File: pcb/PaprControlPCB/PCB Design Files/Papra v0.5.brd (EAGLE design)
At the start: 36 x 45 mm, 40 parts, among them Q1 AO3400A (C20917), Q2 AO3400A (C20917), U1 LP2985-50DBVR (C74511), U2 ATTINYX04SOIC14

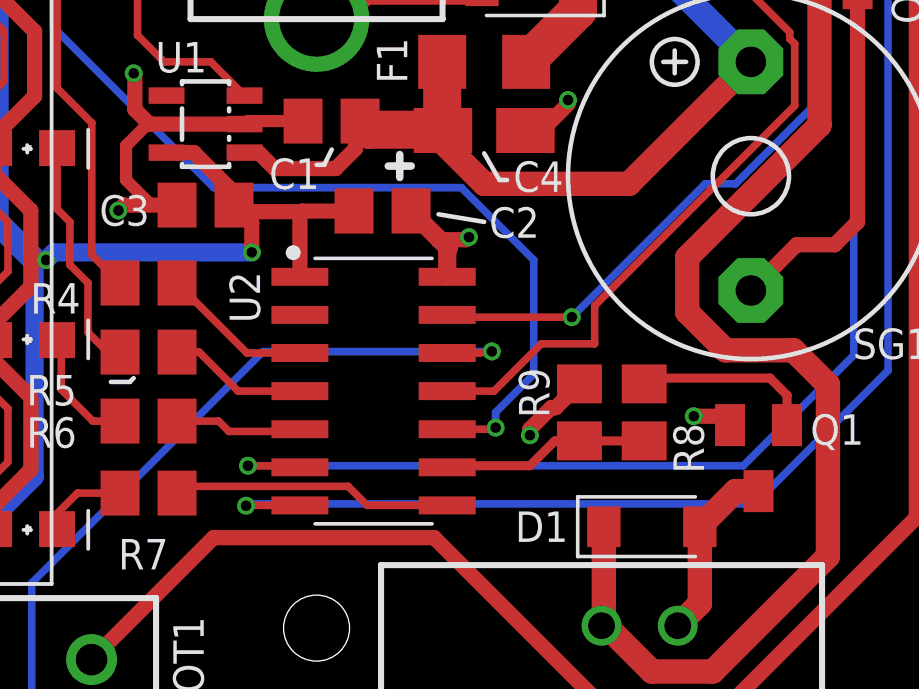
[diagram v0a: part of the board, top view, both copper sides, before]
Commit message: Moved Buzzer to W01 & LED4 to PA4
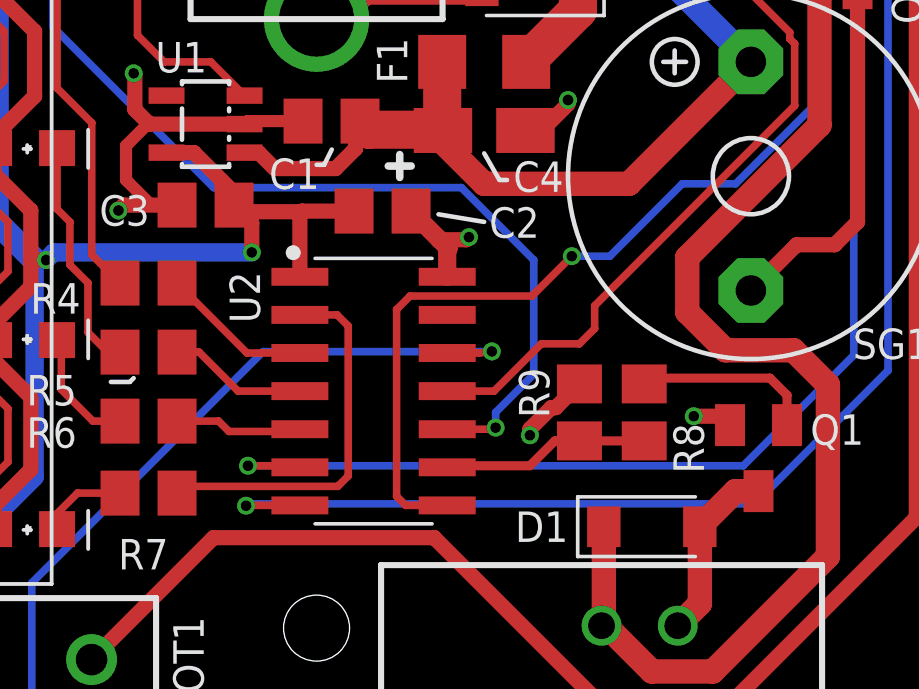
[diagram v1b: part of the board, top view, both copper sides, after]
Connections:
- net BUZZER: now also U2.8; no longer U2.13
- net LED4: now also U2.2; no longer U2.8
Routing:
- net BUZZER: track 28.7 -> 38.3 mm
- net LED4: track 9.36 -> 12.7 mm
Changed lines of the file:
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@@
 <layer number="14" name="Route14" color="22" fill="1" visible="no" active="no"/>
 <layer number="15" name="Route15" color="23" fill="1" visible="no" active="no"/>
-<layer number="16" name="Bottom" color="1" fill="1" visible="no" active="yes"/>
+<layer number="16" name="Bottom" color="1" fill="1" visible="yes" active="yes"/>
 <layer number="17" name="Pads" color="2" fill="1" visible="yes" active="yes"/>
 <layer number="18" name="Vias" color="2" fill="1" visible="yes" active="yes"/>
@@
 <layer number="43" name="vRestrict" color="2" fill="10" visible="no" active="yes"/>
 <layer number="44" name="Drills" color="7" fill="1" visible="no" active="yes"/>
-<layer number="45" name="Holes" color="7" fill="1" visible="no" active="yes"/>
+<layer number="45" name="Holes" color="7" fill="1" visible="yes" active="yes"/>
 <layer number="46" name="Milling" color="3" fill="1" visible="no" active="yes"/>
 <layer number="47" name="Measures" color="7" fill="1" visible="no" active="yes"/>
@@
 </layers>
 <board>
-<fusionsync huburn="a.YnVzaW5lc3M6Z21haWw5OTQ5MjA" projecturn="a.YnVzaW5lc3M6Z21haWw5OTQ5MjAjMjAyMDExMDYzNTA1MTIwMjY" f3durn="urn:adsk.wipprod:dm.lineage:bebFixbaRCeGagELh3PAVg" pcbguid="4d0b5712-029d-481f-ae2c-0115a28a8210" lastpulledtime="" lastsyncedchangeguid="" latestrevisionid="531739e1-a7f7-42f4-b71c-b58853c1dea1" lastsyncedrevisionid="531739e1-a7f7-42f4-b71c-b58853c1dea1" lastboardhashguid="b5928d42-975a-3bc9-637b-dc50c4e995b3" lastpushedtime="2021-04-26T01:24:42Z" linktopcb3d="true"/>
+<fusionsync huburn="a.YnVzaW5lc3M6Z21haWw5OTQ5MjA" projecturn="a.YnVzaW5lc3M6Z21haWw5OTQ5MjAjMjAyMDExMDYzNTA1MTIwMjY" f3durn="urn:adsk.wipprod:dm.lineage:bebFixbaRCeGagELh3PAVg" pcbguid="" lastpulledtime="" lastsyncedchangeguid="" latestrevisionid="531739e1-a7f7-42f4-b71c-b58853c1dea1" lastsyncedrevisionid="531739e1-a7f7-42f4-b71c-b58853c1dea1" lastboardhashguid="b5928d42-975a-3bc9-637b-dc50c4e995b3" lastpushedtime="2021-04-26T01:24:42Z" linktopcb3d="true"/>
 <plain>
 <wire x1="19.5" y1="22.5" x2="-13.5" y2="22.5" width="0.001" layer="20"/>
@@
 <wire x1="15.7734" y1="8.6440625" x2="15.9385" y2="8.4789625" width="0.254" layer="1"/>
 <wire x1="15.9385" y1="8.4789625" x2="15.9385" y2="6.4135" width="0.254" layer="1"/>
-<wire x1="9.271" y1="-0.254" x2="9.271" y2="-1.524" width="0.254" layer="1"/>
+<wire x1="9.271" y1="-0.254" x2="9.271" y2="-1.016" width="0.254" layer="1"/>
+<wire x1="9.271" y1="-1.016" x2="8.763" y2="-1.524" width="0.254" layer="1"/>
+<wire x1="8.763" y1="-1.524" x2="7.493" y2="-1.524" width="0.254" layer="1"/>
 <wire x1="5.917" y1="-3.1" x2="4.3554" y2="-3.1" width="0.254" layer="1"/>
 <wire x1="15.9385" y1="6.4135" x2="9.271" y2="-0.254" width="0.254" layer="1"/>
-<wire x1="9.271" y1="-1.524" x2="7.493" y2="-1.524" width="0.254" layer="1"/>
 <wire x1="7.493" y1="-1.524" x2="5.917" y2="-3.1" width="0.254" layer="1"/>
 </signal>
@@
 <signal name="LED4">
 <contactref element="R7" pad="2"/>
-<contactref element="U2" pad="8"/>
-<wire x1="1.6884" y1="-6.91" x2="4.3554" y2="-6.91" width="0.254" layer="1"/>
-<wire x1="1.6884" y1="-6.91" x2="1.0534" y2="-6.275" width="0.254" layer="1"/>
-<wire x1="1.0534" y1="-6.275" x2="-4.425" y2="-6.275" width="0.254" layer="1"/>
+<wire x1="1.0534" y1="-0.9264" x2="1.0534" y2="-5.9316" width="0.254" layer="1"/>
+<wire x1="1.0534" y1="-5.9316" x2="0.71" y2="-6.275" width="0.254" layer="1"/>
+<wire x1="0.71" y1="-6.275" x2="-4.425" y2="-6.275" width="0.254" layer="1"/>
 <wire x1="-4.65" y1="-6.5" x2="-4.425" y2="-6.275" width="0.254" layer="1"/>
+<contactref element="U2" pad="2"/>
+<wire x1="-0.5554" y1="-0.56" x2="0.687" y2="-0.56" width="0.254" layer="1"/>
+<wire x1="0.687" y1="-0.56" x2="1.0534" y2="-0.9264" width="0.254" layer="1"/>
 </signal>
 <signal name="LED1-R">
@@
 <contactref element="R12" pad="2"/>
 <contactref element="R13" pad="2"/>
-<contactref element="U2" pad="13"/>
 <via x="14.605" y="15.24" extent="1-16" drill="0.35"/>
 <wire x1="14.605" y1="15.24" x2="16.637" y2="13.208" width="0.254" layer="16"/>
-<wire x1="8.509" y1="-0.635" x2="12.954" y2="3.81" width="0.254" layer="16"/>
+<wire x1="12.192" y1="3.81" x2="9.779" y2="1.397" width="0.254" layer="16"/>
+<wire x1="8.509" y1="1.397" x2="9.779" y2="1.397" width="0.254" layer="16"/>
 <wire x1="16.637" y1="13.208" x2="16.637" y2="6.477" width="0.254" layer="16"/>
 <wire x1="16.637" y1="6.477" x2="13.97" y2="3.81" width="0.254" layer="16"/>
-<wire x1="13.97" y1="3.81" x2="12.954" y2="3.81" width="0.254" layer="16"/>
-<via x="8.509" y="-0.635" extent="1-16" drill="0.35"/>
-<wire x1="8.509" y1="-0.635" x2="4.4304" y2="-0.635" width="0.254" layer="1"/>
-<wire x1="4.4304" y1="-0.635" x2="4.3554" y2="-0.56" width="0.254" layer="1"/>
+<wire x1="13.97" y1="3.81" x2="12.192" y2="3.81" width="0.254" layer="16"/>
+<via x="8.509" y="1.397" extent="1-16" drill="0.35"/>
 <wire x1="16.068" y1="14.986" x2="15.814" y2="15.24" width="0.254" layer="1"/>
 <wire x1="15.814" y1="15.24" x2="14.605" y2="15.24" width="0.254" layer="1"/>
 <wire x1="16.068" y1="17.272" x2="16.068" y2="14.986" width="0.3048" layer="1"/>
+<contactref element="U2" pad="8"/>
+<wire x1="4.3554" y1="-6.91" x2="2.973" y2="-6.91" width="0.254" layer="1"/>
+<wire x1="2.973" y1="-6.91" x2="2.667" y2="-6.604" width="0.254" layer="1"/>
+<wire x1="2.667" y1="-6.604" x2="2.667" y2="-0.381" width="0.254" layer="1"/>
+<wire x1="3.11775" y1="0.06975" x2="7.18175" y2="0.06975" width="0.254" layer="1"/>
+<wire x1="7.18175" y1="0.06975" x2="8.509" y2="1.397" width="0.254" layer="1"/>
+<wire x1="2.667" y1="-0.381" x2="3.11775" y2="0.06975" width="0.254" layer="1"/>
 </signal>
 <signal name="BUZZER-GND" class="1">

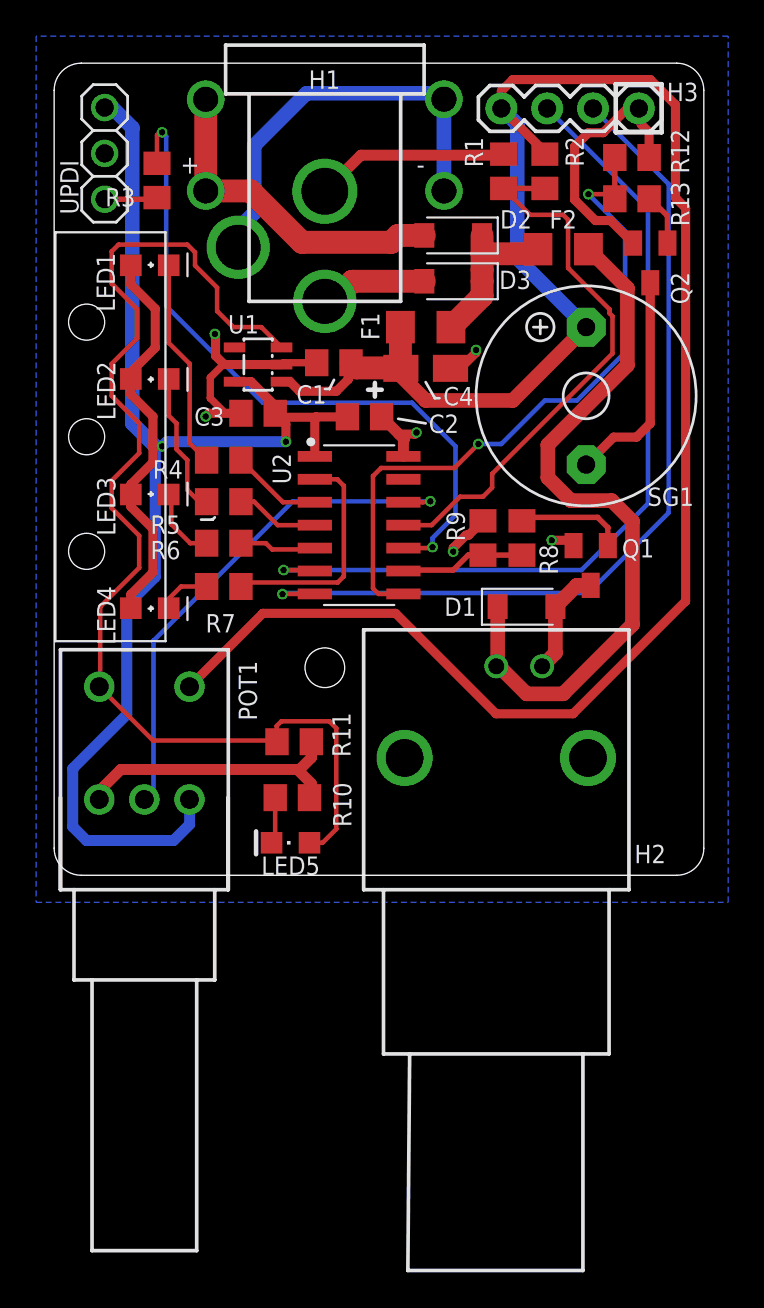
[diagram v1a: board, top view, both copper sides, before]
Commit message: Releasing to OSH
- Fixed for JLC DRU
- Unused pin tied to via & labeled PA3
- Adding 2 vias to allow shorting the UPDI resistor for use with programmers that have the UPDI in-circuit
- Tied the posts on the BNC together (can't tie to ground as we are switching ground)
- Silkscreen touchups
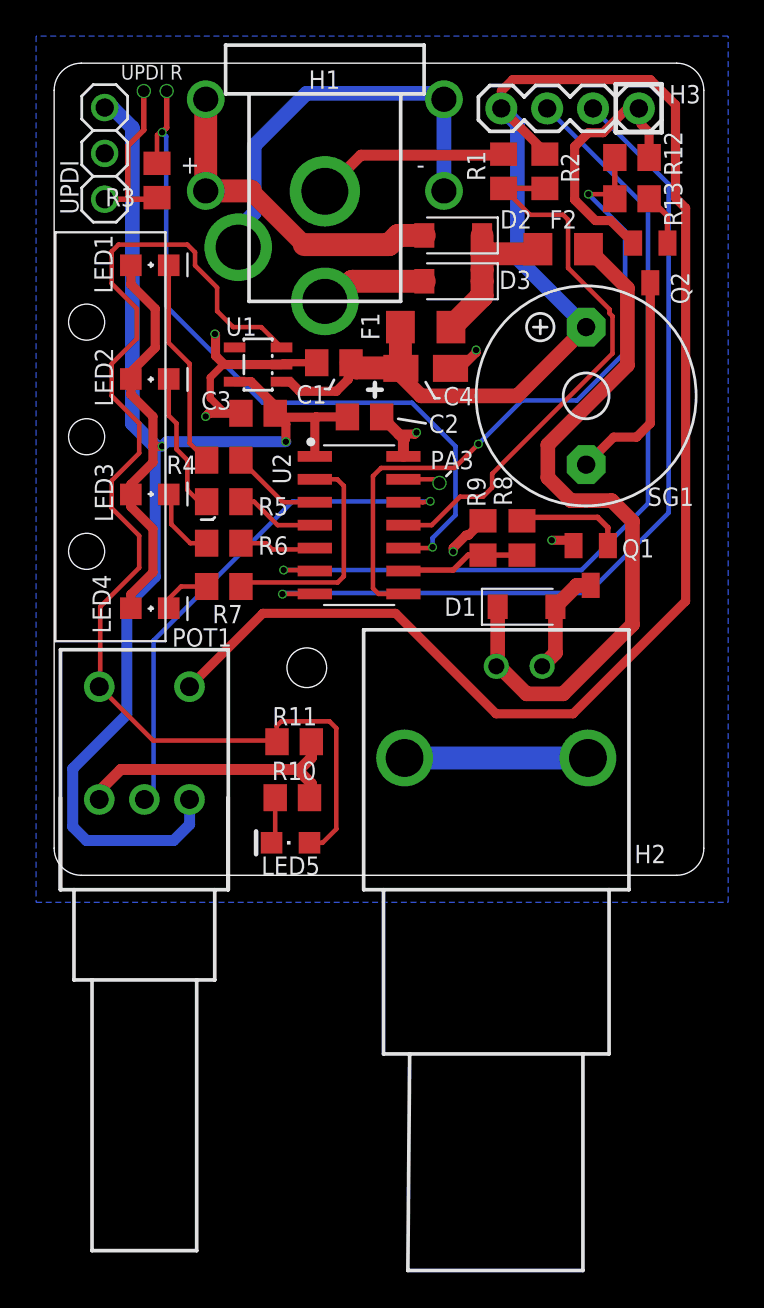
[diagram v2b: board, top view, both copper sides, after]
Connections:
- new net PINS: H2.P$1, H2.P$2
- new net UNUSED: U2.13
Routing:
- net PINS: track 0.00 -> 10.2 mm
- net UPDI: track 2.94 -> 9.30 mm, vias 0 -> 1
- net UPDI/RST: track 38.6 -> 41.0 mm, vias 2 -> 3
- net UNUSED: track 0.00 -> 2.08 mm, vias 0 -> 1
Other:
- board text added: "PA3"
- board text added: "UPDI R"

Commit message: File cleanup
Adding in JLC production files, updated BOMs and resolved conflict
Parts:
- LED1, LED2, LED3, LED4: value NCD0603G1 C84267 -> NCD0805G1 C84260
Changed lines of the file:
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@@
 <layer number="46" name="Milling" color="3" fill="1" visible="no" active="yes"/>
 <layer number="47" name="Measures" color="7" fill="1" visible="no" active="yes"/>
-<layer number="48" name="Document" color="7" fill="1" visible="no" active="yes"/>
+<layer number="48" name="Document" color="7" fill="1" visible="yes" active="yes"/>
 <layer number="49" name="Reference" color="7" fill="1" visible="no" active="yes"/>
 <layer number="50" name="dxf" color="3" fill="1" visible="no" active="no"/>
@@
 </layers>
 <board>
-<fusionsync huburn="a.YnVzaW5lc3M6Z21haWw5OTQ5MjA" projecturn="a.YnVzaW5lc3M6Z21haWw5OTQ5MjAjMjAyMDExMDYzNTA1MTIwMjY" f3durn="urn:adsk.wipprod:dm.lineage:bebFixbaRCeGagELh3PAVg" pcbguid="" lastpulledtime="" lastsyncedchangeguid="" latestrevisionid="531739e1-a7f7-42f4-b71c-b58853c1dea1" lastsyncedrevisionid="531739e1-a7f7-42f4-b71c-b58853c1dea1" lastboardhashguid="b5928d42-975a-3bc9-637b-dc50c4e995b3" lastpushedtime="2021-04-26T01:24:42Z" linktopcb3d="true"/>
+<fusionsync huburn="a.YnVzaW5lc3M6Z21haWw5OTQ5MjA" projecturn="a.YnVzaW5lc3M6Z21haWw5OTQ5MjAjMjAyMDExMDYzNTA1MTIwMjY" f3durn="urn:adsk.wipprod:dm.lineage:bebFixbaRCeGagELh3PAVg" pcbguid="" lastpulledtime="" lastsyncedchangeguid="" latestrevisionid="8a87e740-4a13-43a4-bfaa-62cf4bd8e90a" lastsyncedrevisionid="8a87e740-4a13-43a4-bfaa-62cf4bd8e90a" lastboardhashguid="4f62f28c-cbbc-57c1-cc38-d74b44086e15" lastpushedtime="2021-05-22T18:39:50Z" linktopcb3d="true"/>
 <plain>
 <wire x1="19.5" y1="22.5" x2="-13.5" y2="22.5" width="0.001" layer="20"/>
@@
 v.4
 - Board is 2mm wider on right side
-- DC power out is now BNC</text>
+- DC power out is now BNC
+v.5
+- Board is wider on right side
+- Added Buzzer and circuitry to drive buzzer
+- Adjusted placment of parts to add buzzer and uncrowd region
+- Rotated H3
+- Grounded isolated pins on BNC</text>
 <hole x="-1" y="-11" drill="2.2"/>
 <circle x="-1" y="-11" radius="2.5" width="0.1524" layer="42"/>
@@
 <attribute name="VALUE" x="18.67" y="23.167" size="1.27" layer="27" rot="R180"/>
 </element>
-<element name="LED2" library="led" library_urn="urn:adsk.eagle:library:259" package="CHIPLED_0805" package3d_urn="urn:adsk.eagle:package:15821/2" value="NCD0603G1 C84267" x="-9.7" y="5" smashed="yes" rot="R270">
+<element name="LED2" library="led" library_urn="urn:adsk.eagle:library:259" package="CHIPLED_0805" package3d_urn="urn:adsk.eagle:package:15821/2" value="NCD0805G1 C84260" x="-9.7" y="5" smashed="yes" rot="R270">
 <attribute name="NAME" x="-11.732" y="3.476" size="1.016" layer="25" font="vector" ratio="12" rot="R90"/>
 <attribute name="POPULARITY" value="52" x="-65.58" y="-40.72" size="1.778" layer="27" rot="R270" display="off"/>
 <attribute name="VALUE" x="-10.97" y="2.46" size="1.27" layer="27"/>
 </element>
-<element name="LED3" library="led" library_urn="urn:adsk.eagle:library:259" package="CHIPLED_0805" package3d_urn="urn:adsk.eagle:package:15821/2" value="NCD0603G1 C84267" x="-9.7" y="-1.4" smashed="yes" rot="R270">
+<element name="LED3" library="led" library_urn="urn:adsk.eagle:library:259" package="CHIPLED_0805" package3d_urn="urn:adsk.eagle:package:15821/2" value="NCD0805G1 C84260" x="-9.7" y="-1.4" smashed="yes" rot="R270">
 <attribute name="NAME" x="-11.732" y="-2.924" size="1.016" layer="25" font="vector" ratio="12" rot="R90"/>
 <attribute name="POPULARITY" value="52" x="-65.58" y="-52.2" size="1.778" layer="27" rot="R270" display="off"/>
@@
 <attribute name="VALUE" x="-0.63" y="-18.16" size="1.27" layer="27" rot="R180"/>
 </element>
-<element name="LED4" library="led" library_urn="urn:adsk.eagle:library:259" package="CHIPLED_0805" package3d_urn="urn:adsk.eagle:package:15821/2" value="NCD0603G1 C84267" x="-9.7" y="-7.7" smashed="yes" rot="R270">
+<element name="LED4" library="led" library_urn="urn:adsk.eagle:library:259" package="CHIPLED_0805" package3d_urn="urn:adsk.eagle:package:15821/2" value="NCD0805G1 C84260" x="-9.7" y="-7.7" smashed="yes" rot="R270">
 <attribute name="NAME" x="-11.859" y="-9.097" size="1.016" layer="25" font="vector" ratio="12" rot="R90"/>
 <attribute name="POPULARITY" value="52" x="-65.58" y="-68.66" size="1.778" layer="27" rot="R270" display="off"/>
 <attribute name="VALUE" x="-10.97" y="-10.24" size="1.27" layer="27"/>
 </element>
-<element name="LED1" library="led" library_urn="urn:adsk.eagle:library:259" package="CHIPLED_0805" package3d_urn="urn:adsk.eagle:package:15821/2" value="NCD0603G1 C84267" x="-9.7" y="11.3" smashed="yes" rot="R270">
+<element name="LED1" library="led" library_urn="urn:adsk.eagle:library:259" package="CHIPLED_0805" package3d_urn="urn:adsk.eagle:package:15821/2" value="NCD0805G1 C84260" x="-9.7" y="11.3" smashed="yes" rot="R270">
 <attribute name="NAME" x="-11.76" y="9.741" size="1.016" layer="25" font="vector" ratio="12" rot="R90"/>
 <attribute name="POPULARITY" value="52" x="-71.93" y="-2.67" size="1.778" layer="27" rot="R270" display="off"/>
